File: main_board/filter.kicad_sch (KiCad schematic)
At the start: 0 parts

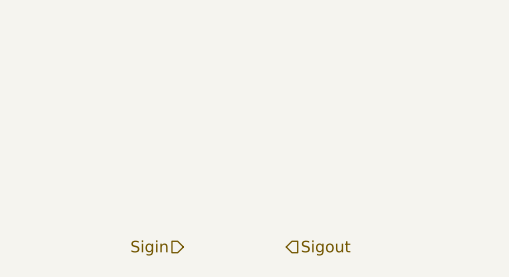
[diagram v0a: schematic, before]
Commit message: bandpass filter added.
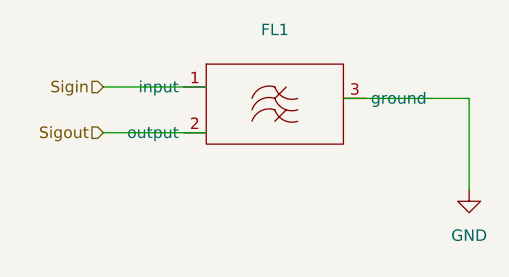
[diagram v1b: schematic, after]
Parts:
- added FL1: ~, 457k_bp_filter_fp:457k_bandpass_FL, symbol bp_filter:457k_bandpass_filter
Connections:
- net Sigin: now also FL1.1 (input)
- net Sigout: now also FL1.2 (output)
- new net GND: FL1.3 (ground)
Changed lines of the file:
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@@
 	(generator_version "9.0")
 	(paper "A4")
+	(wire
+		(pts
+			(xy 74.93 101.6) (xy 74.93 91.44)
+		)
+		(stroke
+			(width 0)
+			(type default)
+		)
+	)
+	(wire
+		(pts
+			(xy 74.93 91.44) (xy 60.96 91.44)
+		)
+		(stroke
+			(width 0)
+			(type default)
+		)
+	)
+	(wire
+		(pts
+			(xy 34.29 90.17) (xy 45.72 90.17)
+		)
+		(stroke
+			(width 0)
+			(type default)
+		)
+	)
+	(wire
+		(pts
+			(xy 34.29 95.25) (xy 45.72 95.25)
+		)
+		(stroke
+			(width 0)
+			(type default)
+		)
+	)
 	(hierarchical_label "Sigout"
 		(shape input)
-		(at 54.61 107.95 0)
-		(effects
-			(font
-				(size 1.27 1.27)
-			)
-			(justify left)
-		)
-	)
-	(hierarchical_label "Sigin"
-		(shape input)
-		(at 43.18 107.95 180)
+		(at 34.29 95.25 180)
 		(effects
 			(font
@@
 		)
 	)
+	(hierarchical_label "Sigin"
+		(shape input)
+		(at 34.29 90.17 180)
+		(effects
+			(font
+				(size 1.27 1.27)
+			)
+			(justify right)
+		)
+	)
+	(symbol
+		(lib_id "power:GND")
+		(at 74.93 101.6 0)
+		(unit 1)
+		(exclude_from_sim no)
+		(in_bom yes)
+		(on_board yes)
+		(dnp no)
+		(fields_autoplaced yes)
+		(property "Reference" "#PWR031"
+			(at 74.93 107.95 0)
+			(effects
+				(font
+					(size 1.27 1.27)
+				)
+				(hide yes)
+			)
+		)
+		(property "Value" "GND"
+			(at 74.93 106.68 0)
+			(effects
+				(font
+					(size 1.27 1.27)
+				)
+			)
+		)
+		(property "Footprint" ""
+			(at 74.93 101.6 0)
+			(effects
+				(font
+					(size 1.27 1.27)
+				)
+				(hide yes)
+			)
+		)
+		(property "Datasheet" ""
+			(at 74.93 101.6 0)
+			(effects
+				(font
+					(size 1.27 1.27)
+				)
+				(hide yes)
+			)
+		)
+		(property "Description" "Power symbol creates a global label with name \"GND\" , ground"
+			(at 74.93 101.6 0)
+			(effects
+				(font
+					(size 1.27 1.27)
+				)
+				(hide yes)
+			)
+		)
+		(pin "1"
+		)
+		(instances
+			(project ""
+				(path "/f3e20914-54f5-4568-9f0b-8875d87df3fb/4b72c036-9d03-4219-91da-5718aacb6260"
+					(reference "#PWR031")
+					(unit 1)
+				)
+			)
+		)
+	)
+	(symbol
+		(lib_id "bp_filter:457k_bandpass_filter")
+		(at 53.34 97.79 0)
+		(unit 1)
+		(exclude_from_sim no)
+		(in_bom yes)
+		(on_board yes)
+		(dnp no)
+		(fields_autoplaced yes)
+		(property "Reference" "FL1"
+			(at 53.34 83.82 0)
+			(effects
+				(font
+					(size 1.27 1.27)
+				)
+			)
+		)
+		(property "Value" "~"
+			(at 53.34 86.36 0)
+			(effects
+				(font
+					(size 1.27 1.27)
+				)
+			)
+		)
+		(property "Footprint" "457k_bp_filter_fp:457k_bandpass_FL"
+			(at 53.34 97.79 0)
+			(effects
+				(font
+					(size 1.27 1.27)
+				)
+				(hide yes)
+			)
+		)
+		(property "Datasheet" ""
+			(at 53.34 97.79 0)
+			(effects
+				(font
+					(size 1.27 1.27)
+				)
+				(hide yes)
+			)
+		)
+		(property "Description" ""
+			(at 53.34 97.79 0)
+			(effects
+				(font
+					(size 1.27 1.27)
+				)
+				(hide yes)
+			)
+		)
+		(pin "1"
+		)
+		(pin "2"
+		)
+		(pin "3"
+		)
+		(instances
+			(project ""
+				(path "/f3e20914-54f5-4568-9f0b-8875d87df3fb/4b72c036-9d03-4219-91da-5718aacb6260"
+					(reference "FL1")
+					(unit 1)
+				)
+			)
+		)
+	)
